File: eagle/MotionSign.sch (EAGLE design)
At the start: 77 parts, among them Q1 16MHZ, U1 ATMEGA328, U2 L7805CDT-TR, U3 NCS36000, U4 PIR, U5 WS2801, U6 SPX3819, U7 NJVMJD2955T4G, U8 TXB0108PWR, U9 LCD-HD4478020X4-4HOLES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

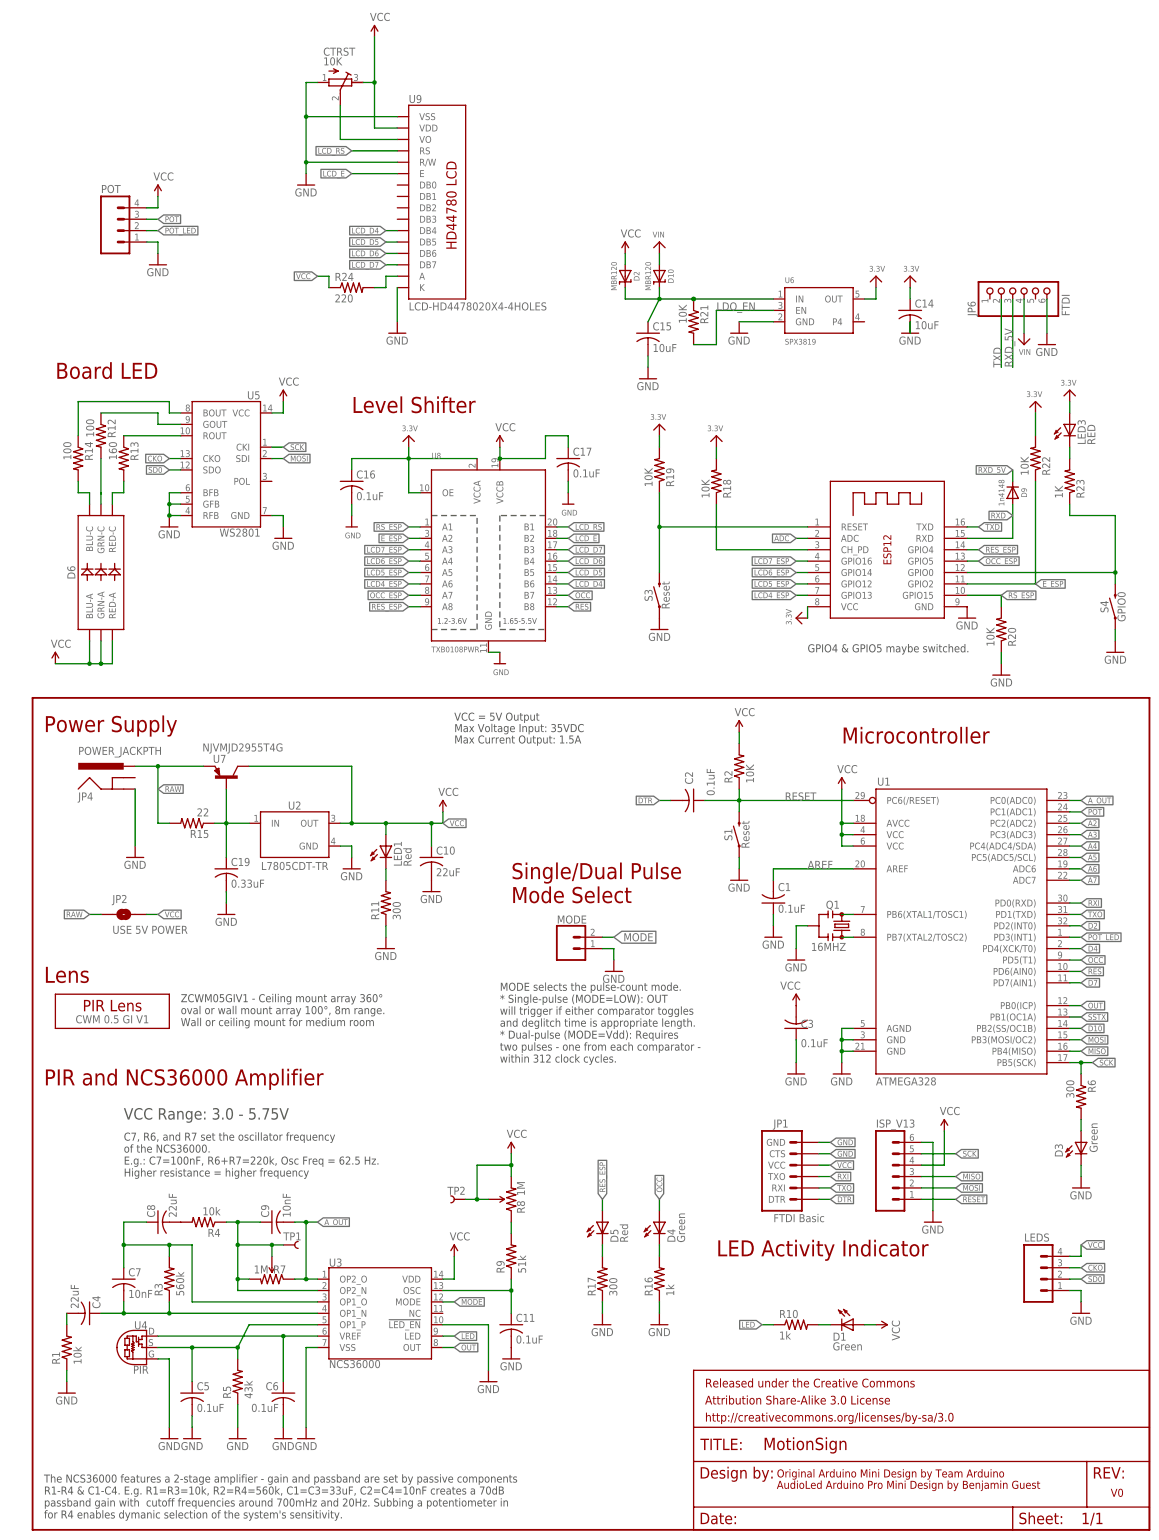
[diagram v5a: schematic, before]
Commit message: Switch to Managed Libary for MotionSign
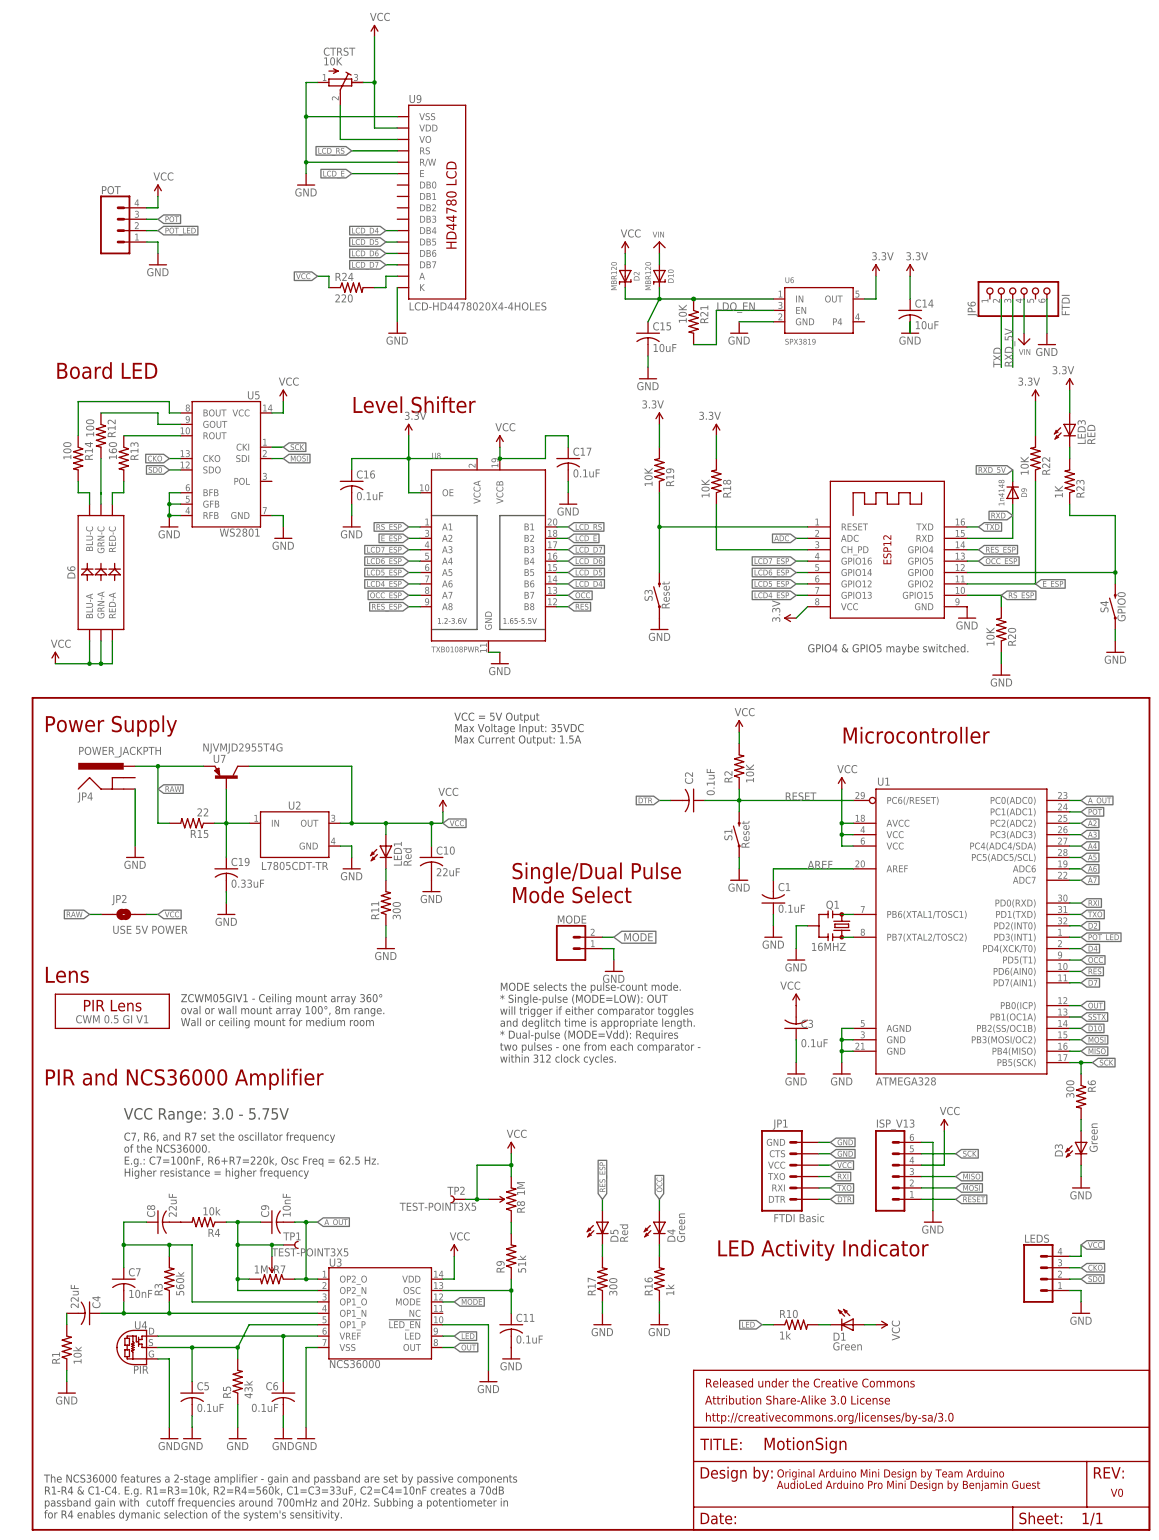
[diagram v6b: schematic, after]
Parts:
- C1, C10, C11, C14, C15, C19, C2, C3, C4, C5, C6, C7, C8, C9: device adafruit:C-USC0805 -> MotionSign:C-USC0805
- CTRST: device resistor:R-TRIMM3296W -> MotionSign:R-TRIMM3296W
- D10, D2: device microbuilder:DIODE-SCHOTTKYSOD-123 -> MotionSign:DIODE-SCHOTTKYSOD-123
- D6: device SparkFun-LED:LED-RGBNO_IC -> MotionSign:LED-RGBNO_IC
- D9: device microbuilder:DIODESOD-323 -> MotionSign:DIODESOD-323
- FRAME1: device SparkFun-Aesthetics:FRAME-LETTER -> MotionSign:FRAME-LETTER
- ISP_V13: device SparkFun-Connectors:M06SIP -> MotionSign:M06SIP
- JP1: device SparkFun:ARDUINO_SERIAL_PROGRAMPTH -> MotionSign:ARDUINO_SERIAL_PROGRAMPTH
- JP2: device SparkFun-Jumpers:JUMPER-SMT_2_NO_SILK -> MotionSign:JUMPER-SMT_2_NO_SILK
- JP4: device SparkFun-Connectors:POWER_JACKPTH -> MotionSign:POWER_JACKPTH
- JP6: device microbuilder:HEADER-1X670MIL -> MotionSign:HEADER-1X670MIL
- LEDS, POT: device SparkFun-Connectors:M04JST-PTH -> MotionSign:CONN_04JST-PTH
- MODE: device SparkFun-Connectors:CONN_02 -> MotionSign:CONN_02
- Q1: device SparkFun-FreqCtrl:RESONATOR16MHZ -> MotionSign:RESONATOR16MHZ
- R1, R10, R11, R12, R13, R14, R15, R16, R17, R18, R19, R2, R20, R21, R22, R23, R3, R4, R5, R6, R9: device adafruit:R-US_M0805 -> MotionSign:R-US_M0805
- R24: device resistor:R-US_0204/7 -> MotionSign:R-US_0204/7
- R7, R8: device openPIR-temp:TRIMPOTTX33X-1M -> MotionSign:TRIMPOTTX33X-1M
- S1, S3, S4: device SparkFun-Switches:MOMENTARY-SWITCH-SPST-SMD-5.2-REDUNDANT -> MotionSign:MOMENTARY-SWITCH-SPST-SMD-5.2-REDUNDANT
- TP1, TP2: device SparkFun-Connectors:TEST-POINT3X5 -> MotionSign:TEST-POINT3X5
- U$1: device openPIR-temp:PIR-LENSCWM-0.5-GI-V1 -> MotionSign:PIR-LENSCWM-0.5-GI-V1
- U1: device SparkFun:ATMEGA168 -> MotionSign:ATMEGA168
- U2: device BAG:L7805CDT-TR -> MotionSign:L7805CDT-TR
- U3: device openPIR-temp:NCS36000 -> MotionSign:NCS36000
- U4: device openPIR-temp:PIR -> MotionSign:PIR
- U5: device SparkFun-DigitalIC:WS2801 -> MotionSign:WS2801
- U6: device microbuilder:VREG_SOT23-5 -> MotionSign:VREG_SOT23-5
- U7: device bg_eagle_lib:NJVMJD2955T4G -> MotionSign:NJVMJD2955T4G
- U8: device microbuilder:TXB0108PWR -> MotionSign:TXB0108PWR
- U9: device HD44780LCD:LCD-HD44780 -> MotionSign:LCD-HD44780
- X2: device microbuilder:ESP-12 -> MotionSign:ESP-12
